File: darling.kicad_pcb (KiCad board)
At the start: 2 copper layers, 24 x 14 mm, 16 parts, among them J1 USB_C_Receptacle_USB2.0, J2 Conn_01x05, U1 FT230XQ

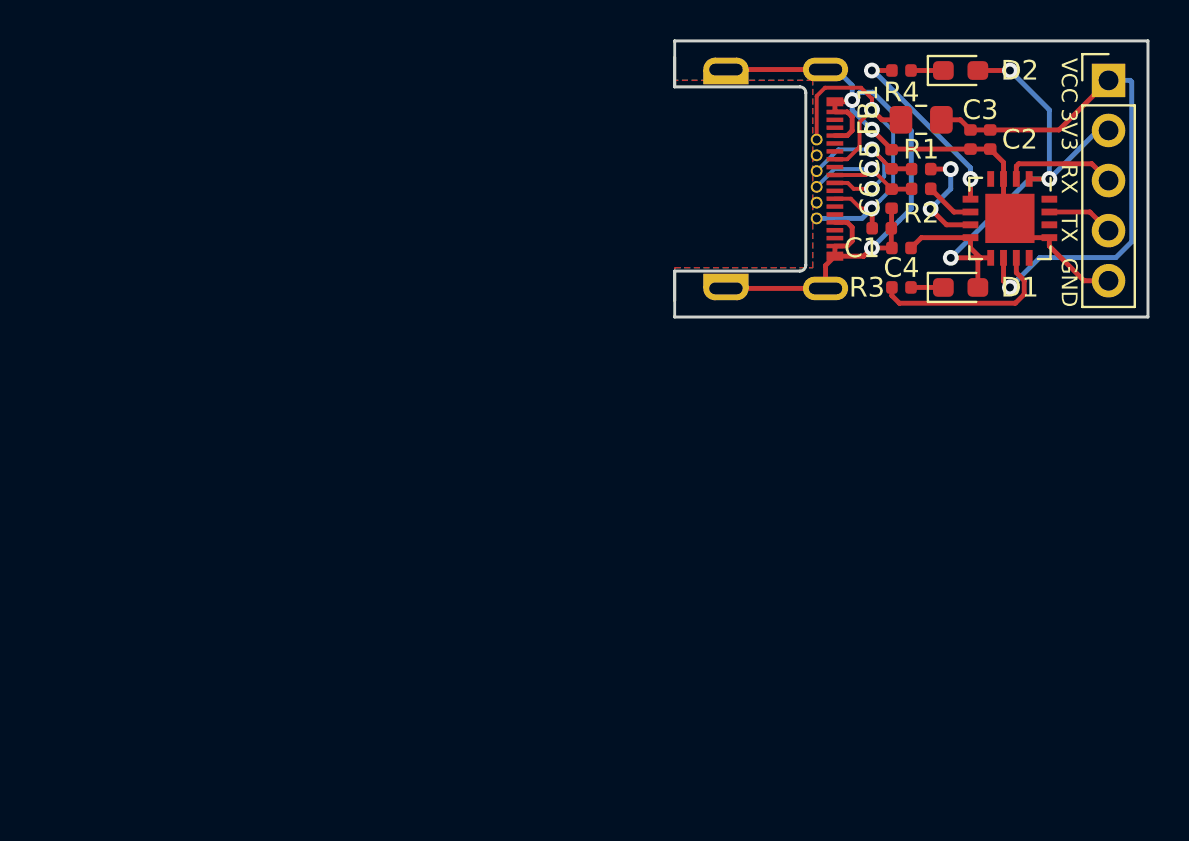
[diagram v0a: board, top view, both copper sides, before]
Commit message: Add missing CC resistors
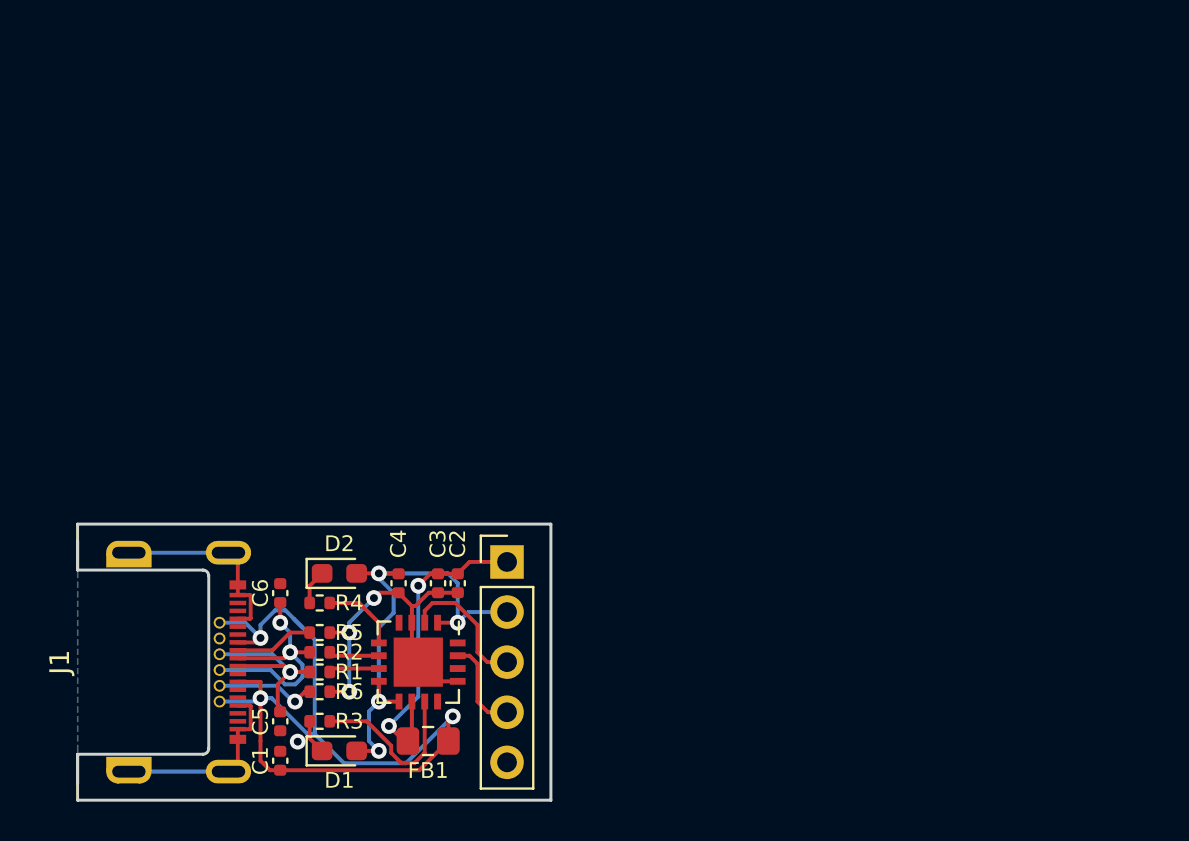
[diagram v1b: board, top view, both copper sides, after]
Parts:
- added G***: LOGO, 002:002, B.Cu at (102.2, 146.9)
- added R5: 5k1, Resistor_SMD:R_0402_1005Metric, F.Cu at (99.0, 146.5)
- added R6: 5k1, Resistor_SMD:R_0402_1005Metric, F.Cu at (99.0, 149.5)
- moved C5 42.1 mm to (97.0, 151.0), turned to -90 degrees
- moved C1 40.7 mm to (97.0, 153.0), turned to 90 degrees
- moved D2 40.5 mm to (100.0, 143.5)
- moved FB1 40.2 mm to (104.5, 152.0), turned to 0 degrees
- moved R4 40.0 mm to (99.0, 145.0), turned to 0 degrees
- moved R1 39.8 mm to (99.0, 148.5)
- moved D1 39.3 mm to (100.0, 152.5)
- moved J2 39.1 mm to (108.5, 142.9)
- moved J1 38.9 mm to (86.7, 148.0)
- moved R2 38.5 mm to (99.0, 147.5)
- moved U1 37.5 mm to (104.0, 148.0)
- moved C6 36.9 mm to (97.0, 144.5), turned to 90 degrees
- moved R3 36.8 mm to (99.0, 151.0), turned to 0 degrees
- moved C2 35.1 mm to (106.0, 144.0)
- moved C3 35.1 mm to (105.0, 144.0)
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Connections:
- net 3V3 renamed VCCIO
- net VCC renamed +5V
- J1 pad A8: Net-(J1-PadA8) -> unconnected-(J1-SBU1-PadA8)
- J1 pad B8: Net-(J1-PadB8) -> unconnected-(J1-SBU2-PadB8)
- U1 pad 12: Net-(U1-Pad12) -> unconnected-(U1-CBUS0-Pad12)
- U1 pad 14: Net-(U1-Pad14) -> unconnected-(U1-CBUS3-Pad14)
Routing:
- net Net-(C1-Pad1): track 23.3 -> 44.4 mm, vias 2 -> 3
- net GND: track 56.5 -> 37.3 mm, vias 3 -> 4
- net +5V: track 27.8 -> 16.1 mm, vias 1 -> 2
- net /TXLED: track 9.65 -> 3.93 mm, vias 2 -> 0
- net Net-(J1-CC2): track 0.00 -> 5.10 mm, vias 0 -> 1
- net Net-(C6-Pad1): track 7.79 -> 12.7 mm, vias 1 -> 2
- net Net-(J1-CC1): track 0.00 -> 4.01 mm
- net Net-(U1-USBDM): track 5.81 -> 2.56 mm, vias 2 -> 0
- net VCCIO: track 27.7 -> 25.3 mm, vias 3 -> 4
- net TX: track 3.39 -> 4.81 mm
- net RX: track 5.73 -> 7.00 mm
- net /RXLED: track 9.49 -> 8.70 mm
- net Net-(C5-Pad1): track 10.3 -> 10.0 mm, vias 2 -> 1
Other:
- outline, holes or cut-outs redrawn
- net class Default removed
- net class GND removed
- board text added: "5V"
- board text added: "G"
- board text added: "darling.xengi.de rev4"
- board text removed: "GND"
- board text removed: "VCC"
- board text removed: "darling.xengi.de"

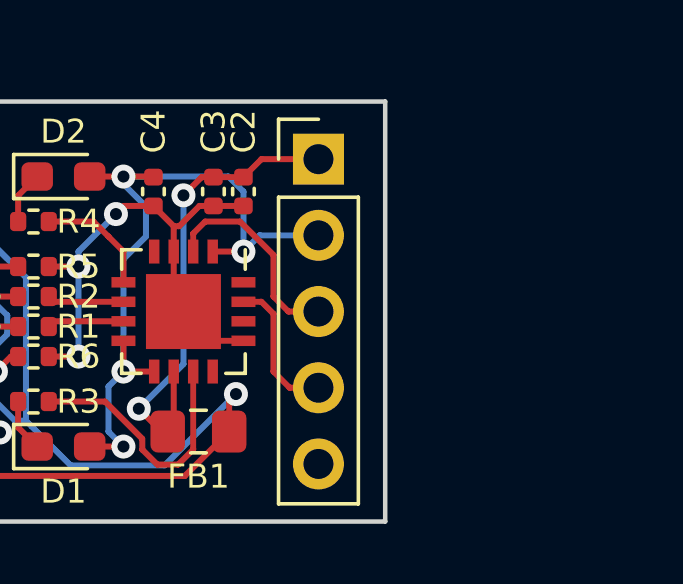
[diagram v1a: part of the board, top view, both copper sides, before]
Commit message: update pictures
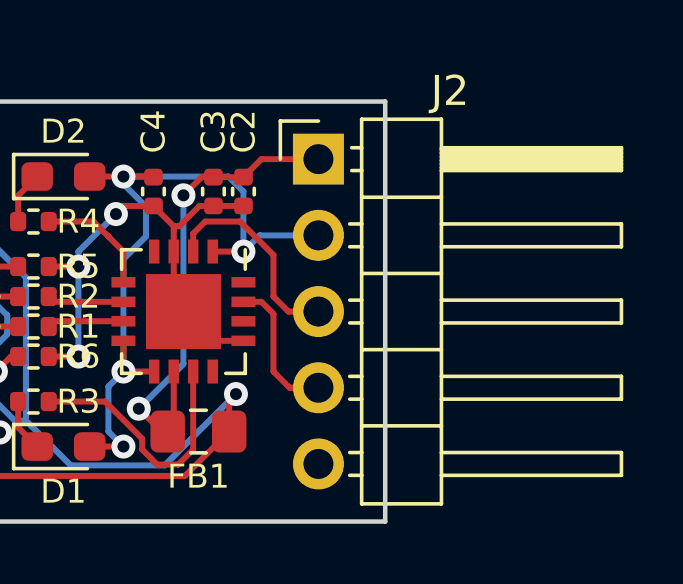
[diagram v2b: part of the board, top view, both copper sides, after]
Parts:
- J2: footprint Connector_PinHeader_2.54mm:PinHeader_1x05_P2.54mm_Vertical -> Connector_PinHeader_2.54mm:PinHeader_1x05_P2.54mm_Horizontal

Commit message: minimal touches
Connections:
- net +5V renamed VCC
- net CTS renamed /CTS
- net RTS renamed /RTS
- net RX renamed /RX
- net TX renamed /TX
- net VCCIO renamed +3V3
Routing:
- net /RX: track 7.00 -> 6.42 mm
